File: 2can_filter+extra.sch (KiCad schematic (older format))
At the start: 25 parts, among them J5 54819-0572, J6 NOT_FITTED_SWD_Conn_01x04_Male, U10 74HC4050D, U11 TJA1040T, U12 TJA1040T, U8 74HC4050D, U9 STM32F105RBTx, Y2 Crystal KX-13 25MHz

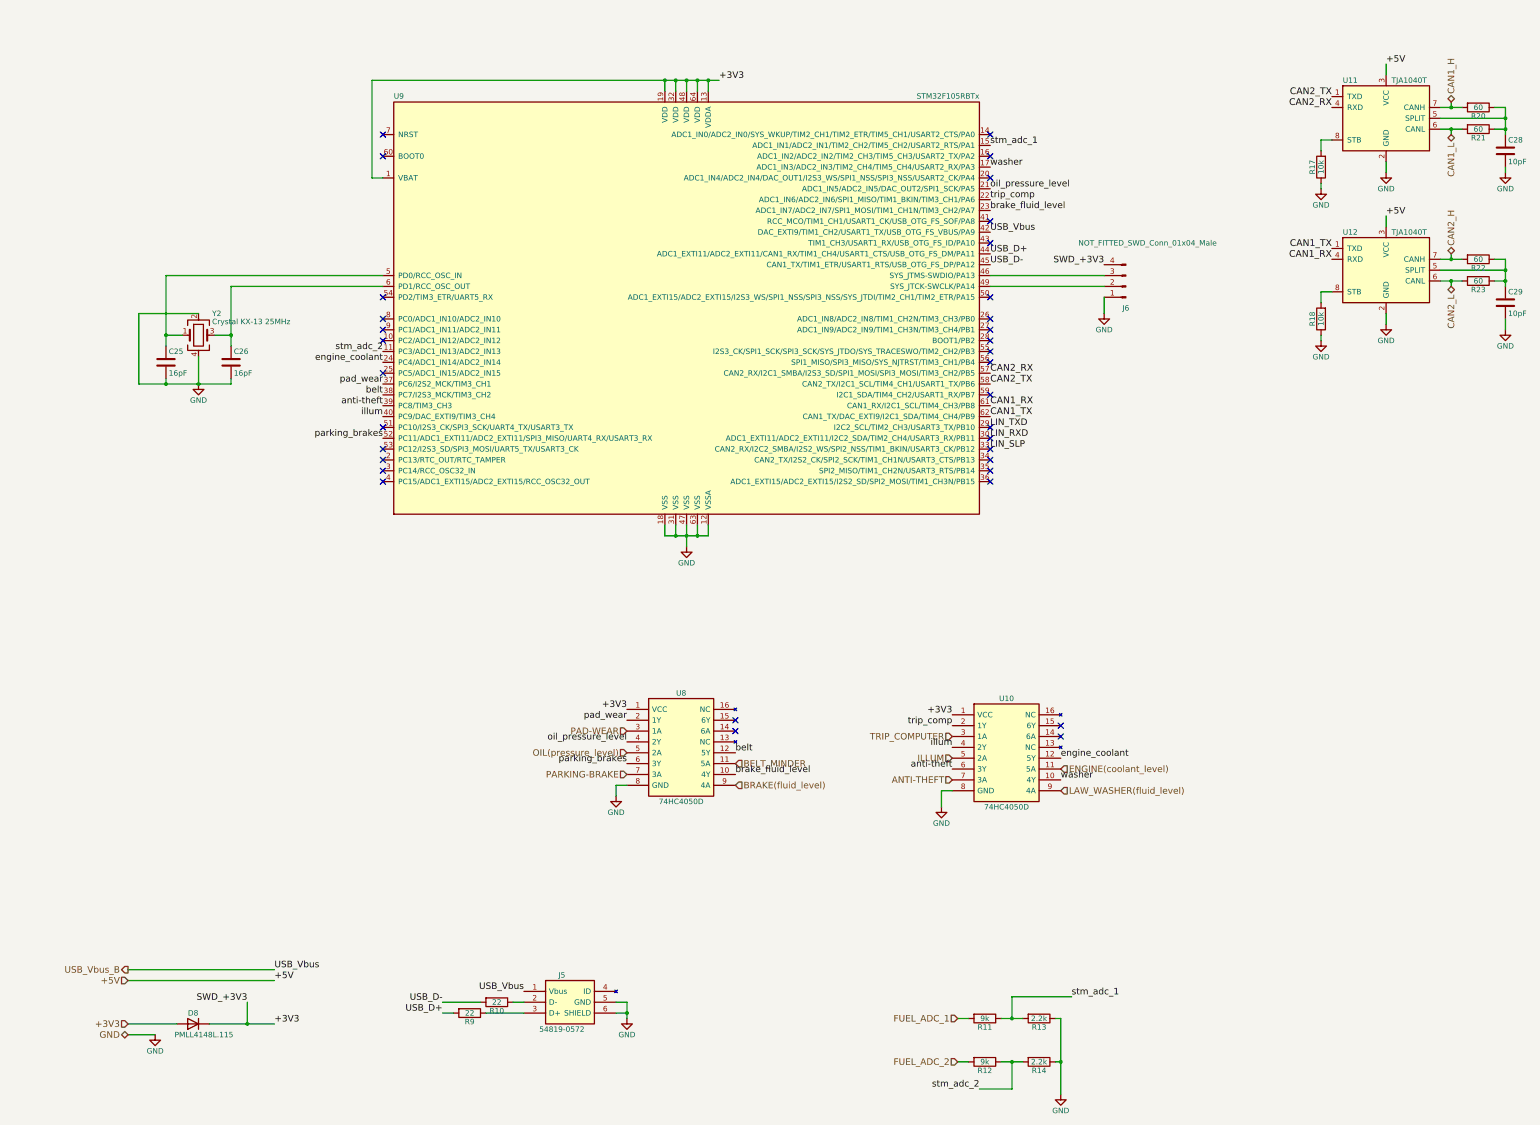
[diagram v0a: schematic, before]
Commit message: change connectivity of level-shifters(on sheme and pcb)
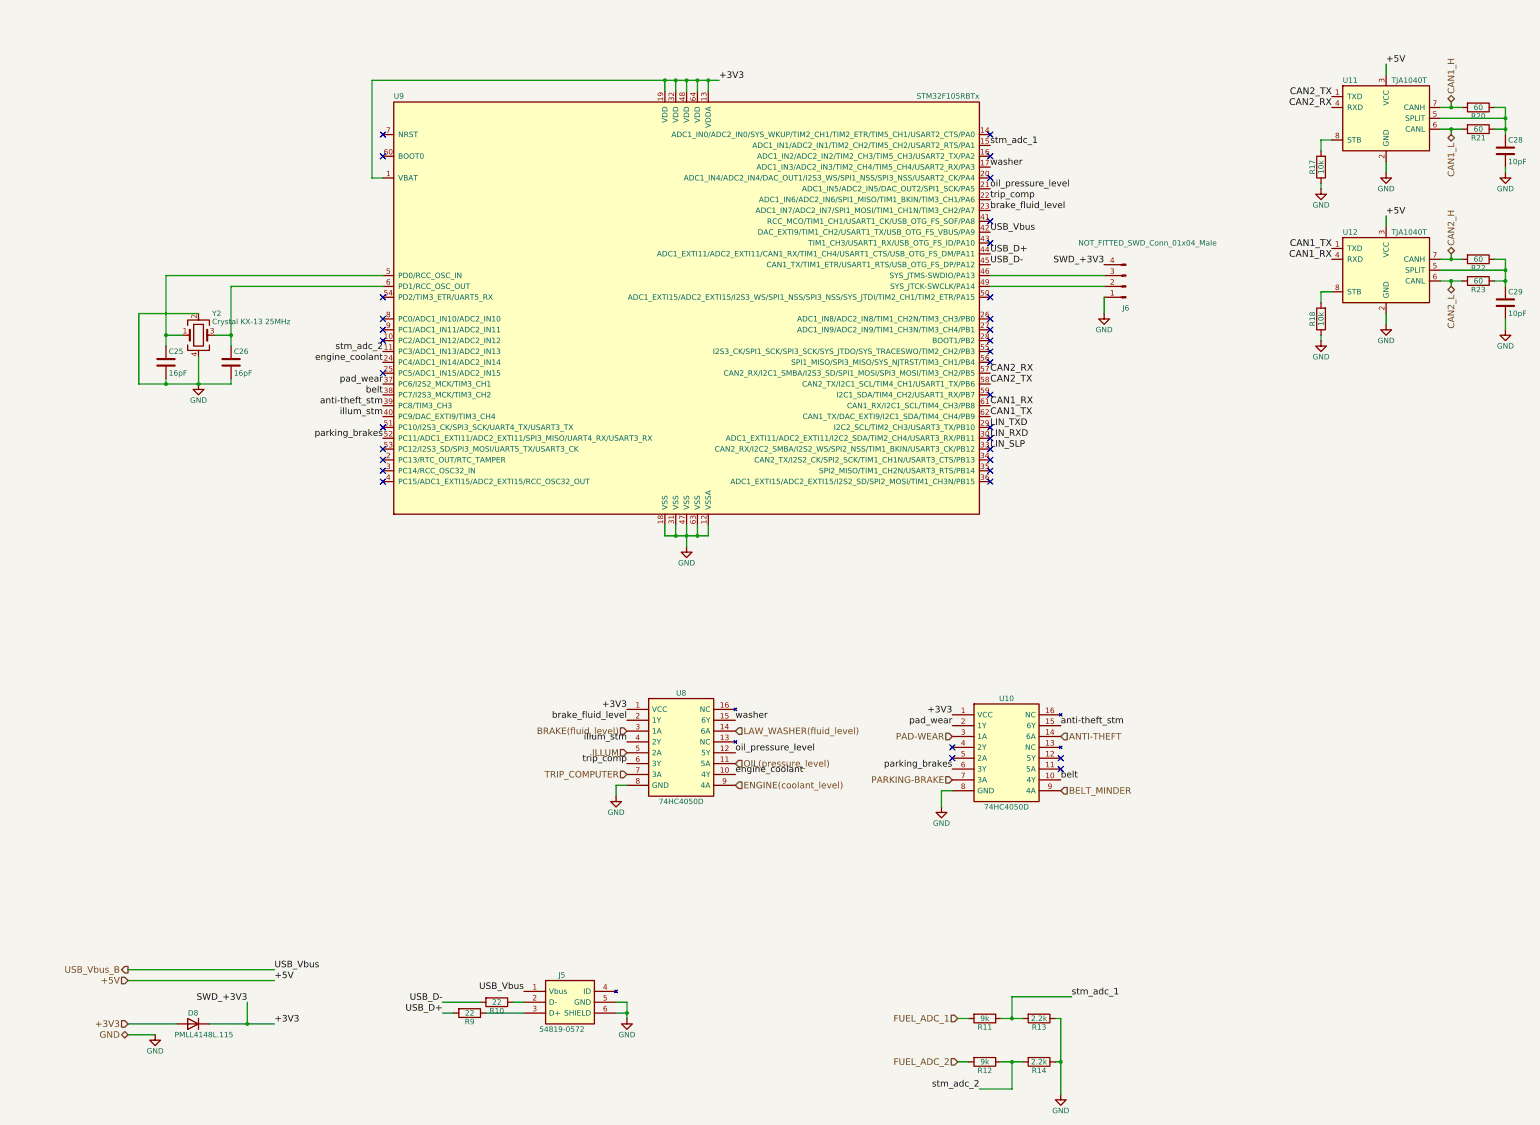
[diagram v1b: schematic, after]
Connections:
- net ANTI-THEFT: now also U10.14 (6A); no longer U10.7 (3A)
- net BELT_MINDER: now also U10.9 (4A); no longer U8.11 (5A)
- net BRAKE(fluid_level): now also U8.3 (1A); no longer U8.9 (4A)
- net ENGINE(coolant_level): now also U8.9 (4A); no longer U10.11 (5A)
- net ILLUM: now also U8.5 (2A); no longer U10.5 (2A)
- net LAW_WASHER(fluid_level): now also U8.14 (6A); no longer U10.9 (4A)
- net OIL(pressure_level): now also U8.11 (5A); no longer U8.5 (2A)
- net PAD-WEAR: now also U10.3 (1A); no longer U8.3 (1A)
- net PARKING-BRAKE: now also U10.7 (3A); no longer U8.7 (3A)
- net TRIP_COMPUTER: now also U8.7 (3A); no longer U10.3 (1A)
- net belt: now also U10.10 (4Y); no longer U8.12 (5Y)
- net brake_fluid_level: now also U8.2 (1Y); no longer U8.10 (4Y)
- net engine_coolant: now also U8.10 (4Y); no longer U10.12 (5Y)
- net oil_pressure_level: now also U8.12 (5Y); no longer U8.4 (2Y)
- net pad_wear: now also U10.2 (1Y); no longer U8.2 (1Y)
- net parking_brakes: now also U10.6 (3Y); no longer U8.6 (3Y)
- net trip_comp: now also U8.6 (3Y); no longer U10.2 (1Y)
- net washer: now also U8.15 (6Y); no longer U10.10 (4Y)
- net anti-theft_stm: now reaches U10.15 (6Y)
- net anti-theft_stm: now also U9.39 (PC8/TIM3_CH3)
- removed net anti-theft: U10.6 (3Y), U9.39 (PC8/TIM3_CH3)
- net illum: no longer names the net of U10.4 (2Y)
- net illum: no longer U9.40 (PC9/DAC_EXTI9/TIM3_CH4)
- new net illum_stm: U8.4 (2Y), U9.40 (PC9/DAC_EXTI9/TIM3_CH4)
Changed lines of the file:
@@
 $EndComp
 Wire Wire Line
-	13900 1500 14000 1500
-Wire Wire Line
-	14000 1500 14100 1500
+	13900 1500 14100 1500
 Wire Wire Line
 	14000 1450 14000 1500
@@
 $EndComp
 Wire Wire Line
-	4050 1250 6750 1250
-Wire Wire Line
-	6750 1250 6850 1250
-Wire Wire Line
-	6850 1250 6950 1250
-Wire Wire Line
-	6950 1250 7050 1250
-Wire Wire Line
-	7050 1250 7150 1250
-Wire Wire Line
-	7150 1250 7250 1250
+	4050 1250 7250 1250
 Wire Wire Line
 	7150 1250 7150 1350
@@
 	6750 5350 6750 5450
 Wire Wire Line
-	6750 5450 6850 5450
-Wire Wire Line
-	6850 5450 6950 5450
-Wire Wire Line
-	6950 5450 7050 5450
-Wire Wire Line
-	7050 5450 7150 5450
+	6750 5450 7150 5450
 Wire Wire Line
 	7150 5450 7150 5350
@@
 Connection ~ 7050 5450
 Wire Wire Line
-	6950 5350 6950 5450
-Wire Wire Line
-	6950 5450 6950 5550
+	6950 5350 6950 5550
 Connection ~ 6950 5450
 Wire Wire Line
@@
 +3V3
 Wire Wire Line
-	13900 1700 14000 1700
-Wire Wire Line
-	14000 1700 14100 1700
+	13900 1700 14100 1700
 Wire Wire Line
 	14000 1750 14000 1700
@@
 	13900 1600 14500 1600
 Wire Wire Line
-	14500 1500 14500 1600
-Wire Wire Line
-	14500 1600 14500 1700
-Wire Wire Line
-	14500 1700 14500 1750
+	14500 1500 14500 1750
 Wire Wire Line
 	14500 1700 14400 1700
@@
 	13900 3000 14500 3000
 Wire Wire Line
-	14500 2900 14500 3000
-Wire Wire Line
-	14500 3000 14500 3100
-Wire Wire Line
-	14500 3100 14500 3150
+	14500 2900 14500 3150
 Wire Wire Line
 	14500 3100 14400 3100
@@
 Connection ~ 14500 3000
 Wire Wire Line
-	13900 2900 14000 2900
-Wire Wire Line
-	14000 2900 14100 2900
+	13900 2900 14100 2900
 Wire Wire Line
 	14000 2850 14000 2900
 Connection ~ 14000 2900
 Wire Wire Line
-	13900 3100 14000 3100
-Wire Wire Line
-	14000 3100 14100 3100
+	13900 3100 14100 3100
 Wire Wire Line
 	14000 3150 14000 3100
@@
 SWD_+3V3
 Wire Wire Line
-	2550 9950 2900 9950
-Wire Wire Line
-	2900 9950 3150 9950
+	2550 9950 3150 9950
 Wire Wire Line
 	2900 9750 2900 9950
@@
 	2750 4050 2750 4000
 Wire Wire Line
-	2150 3050 2150 3600
-Wire Wire Line
-	2150 3600 2150 3700
+	2150 3050 2150 3700
 Wire Wire Line
 	2150 3600 2300 3600
@@
 	2600 3600 2750 3600
 Wire Wire Line
-	2750 3150 2750 3600
-Wire Wire Line
-	2750 3600 2750 3700
+	2750 3150 2750 3700
 Connection ~ 2150 3600
 Connection ~ 2750 3600
@@
 	6300 9750 6400 9750
 Wire Wire Line
-	6400 9750 6400 9850
-Wire Wire Line
-	6400 9850 6400 9900
+	6400 9750 6400 9900
+Text HLabel 6400 7650 0    60   Input ~ 0
+TRIP_COMPUTER
+Text HLabel 6400 7450 0    60   Input ~ 0
+ILLUM
+Text HLabel 10400 7300 2    60   Input ~ 0
+ANTI-THEFT
 Text HLabel 9400 7300 0    60   Input ~ 0
-TRIP_COMPUTER
-Text HLabel 9400 7500 0    60   Input ~ 0
-ILLUM
+PAD-WEAR
+Text HLabel 7400 7550 2    60   Input ~ 0
+OIL(pressure_level)
 Text HLabel 9400 7700 0    60   Input ~ 0
-ANTI-THEFT
-Text HLabel 6400 7250 0    60   Input ~ 0
-PAD-WEAR
-Text HLabel 6400 7450 0    60   Input ~ 0
-OIL(pressure_level)
-Text HLabel 6400 7650 0    60   Input ~ 0
 PARKING-BRAKE
 Text HLabel 9450 9900 0    60   Input ~ 0
@@
 Text HLabel 9450 10300 0    60   Input ~ 0
 FUEL_ADC_2
-Text HLabel 10400 7600 2    60   Input ~ 0
+Text HLabel 7400 7750 2    60   Input ~ 0
 ENGINE(coolant_level)
+Text HLabel 7400 7250 2    60   Input ~ 0
+LAW_WASHER(fluid_level)
+Text HLabel 6400 7250 0    60   Input ~ 0
+BRAKE(fluid_level)
 Text HLabel 10400 7800 2    60   Input ~ 0
-LAW_WASHER(fluid_level)
-Text HLabel 7400 7750 2    60   Input ~ 0
-BRAKE(fluid_level)
-Text HLabel 7400 7550 2    60   Input ~ 0
 BELT_MINDER
 Text Label 9400 7100 2    60   ~ 0
@@
 $EndComp
 Wire Wire Line
-	9850 9900 9950 9900
-Wire Wire Line
-	9950 9900 10050 9900
+	9850 9900 10050 9900
 Wire Wire Line
 	9550 9900 9450 9900
@@
 $EndComp
 Wire Wire Line
-	9850 10300 9950 10300
-Wire Wire Line
-	9950 10300 10050 10300
+	9850 10300 10050 10300
 Wire Wire Line
 	9550 10300 9450 10300
@@
 $EndComp
 Wire Wire Line
-	10400 9900 10400 10300
-Wire Wire Line
-	10400 10300 10400 10600
+	10400 9900 10400 10600
 Connection ~ 10400 10300
 Text Label 10500 9700 0    60   ~ 0
@@
 Wire Wire Line
 	2750 3150 4150 3150
-NoConn ~ 10400 7300
-NoConn ~ 10400 7200
-NoConn ~ 7400 7250
-NoConn ~ 7400 7150
-Text Label 9400 7200 2    60   ~ 0
+Text Label 6400 7550 2    60   ~ 0
 trip_comp
-Text Label 9400 7400 2    60   ~ 0
-illum
-Text Label 9400 7600 2    60   ~ 0
-anti-theft
+Text Label 6400 7350 2    60   ~ 0
+illum_stm
+Text Label 10400 7200 0    60   ~ 0
+anti-theft_stm
 $Comp
 L GND #PWR043
@@
 Wire Wire Line
 	6300 7750 6400 7750
+Text Label 7400 7150 0    60   ~ 0
+washer
+Text Label 7400 7650 0    60   ~ 0
+engine_coolant
 Text Label 10400 7700 0    60   ~ 0
-washer
-Text Label 10400 7500 0    60   ~ 0
-engine_coolant
+belt
+Text Label 6400 7150 2    60   ~ 0
+brake_fluid_level
+Text Label 9400 7600 2    60   ~ 0
+parking_brakes
+Text Label 9400 7200 2    60   ~ 0
+pad_wear
 Text Label 7400 7450 0    60   ~ 0
-belt
-Text Label 7400 7650 0    60   ~ 0
-brake_fluid_level
-Text Label 6400 7550 2    60   ~ 0
-parking_brakes
-Text Label 6400 7150 2    60   ~ 0
-pad_wear
-Text Label 6400 7350 2    60   ~ 0
 oil_pressure_level
 Text Label 4150 4550 2    60   ~ 0
@@
 trip_comp
 Text Label 4150 4250 2    60   ~ 0
-anti-theft
-Text Label 4150 4350 2    60   ~ 0
-illum
+anti-theft_stm
 NoConn ~ 4150 4650
 NoConn ~ 4150 4750
@@
 	2450 4050 2450 3800
 Wire Wire Line
-	1900 4050 2150 4050
-Wire Wire Line
-	2150 4050 2450 4050
-Wire Wire Line
-	2450 4050 2750 4050
+	1900 4050 2750 4050
 Connection ~ 2450 4050
 Wire Wire Line
@@
 Text Label 4150 3750 2    60   ~ 0
 stm_adc_2
+NoConn ~ 9400 7400
+NoConn ~ 9400 7500
+NoConn ~ 10400 7500
+NoConn ~ 10400 7600
+Text Label 4150 4350 2    60   ~ 0
+illum_stm
 $EndSCHEMATC

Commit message: redone shematic of power supply, fix usb_vbus and swd diods connections, change mcu capacitors connections
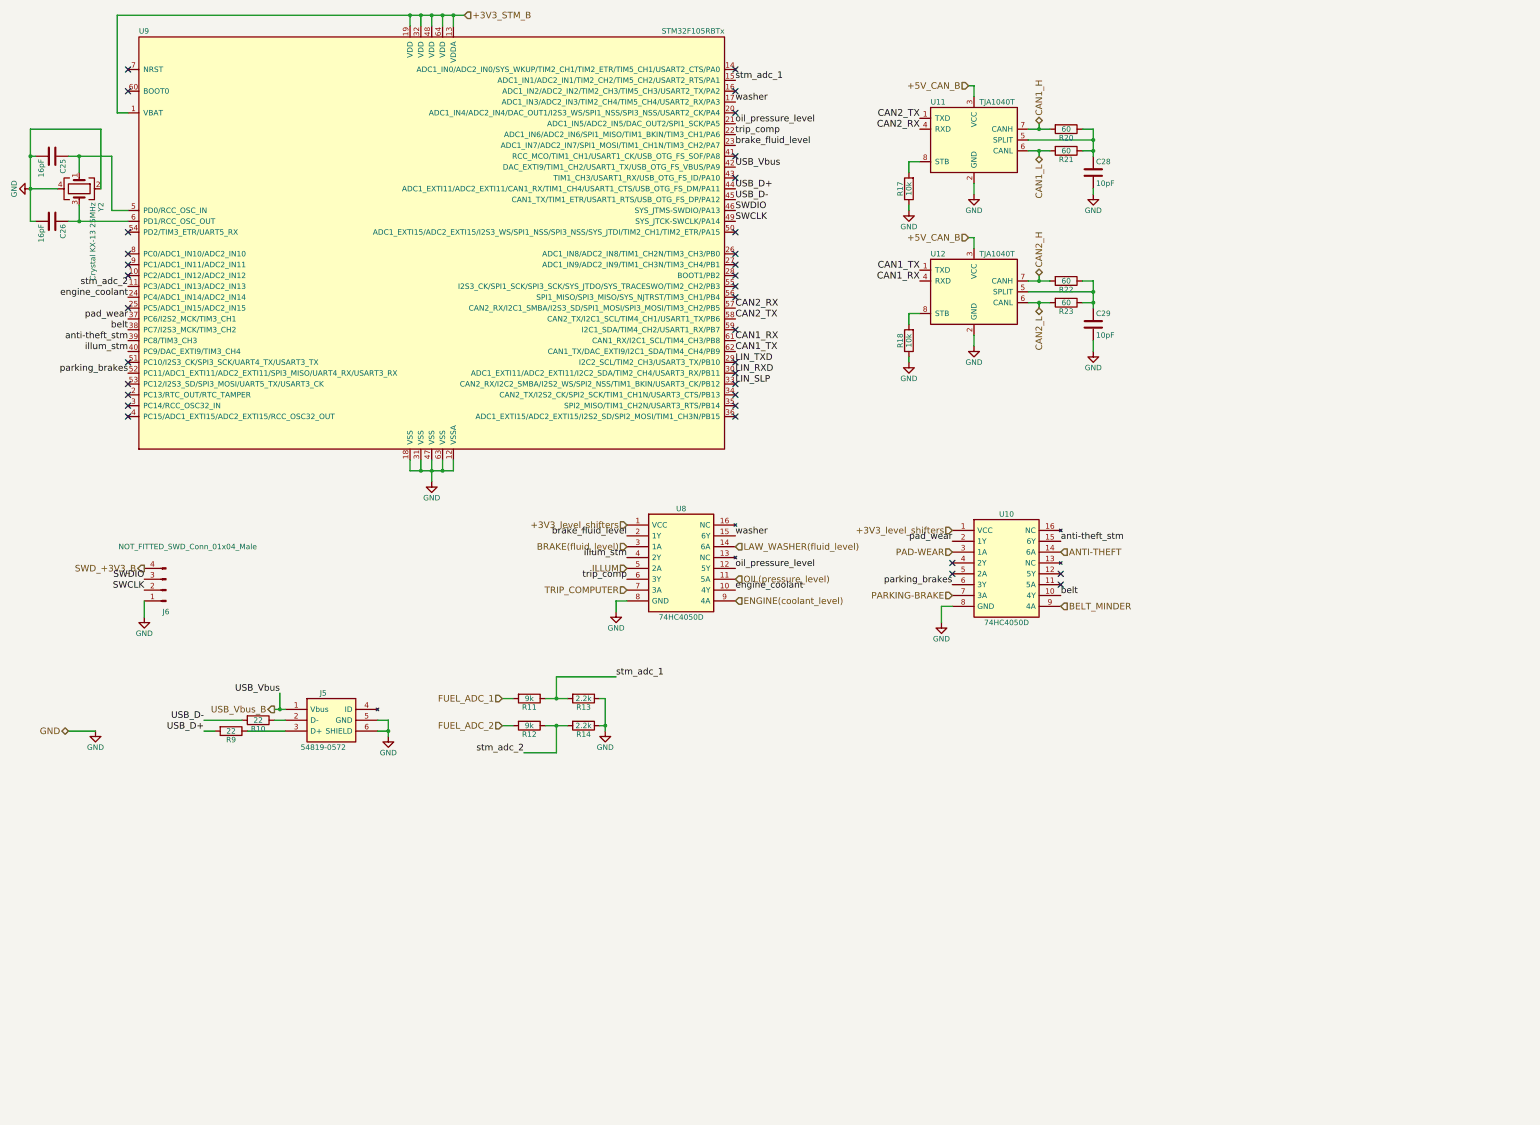
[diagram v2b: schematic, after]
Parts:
- removed D8: PMLL4148L.115, Diodes_SMD:D_SC-80, symbol D
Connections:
- net SWDIO: now reaches J6.3 (Pin_3), U9.46 (SYS_JTMS-SWDIO/PA13)
- net SWCLK: now reaches J6.2 (Pin_2), U9.49 (SYS_JTCK-SWCLK/PA14)
- net +3V3 renamed +3V3_STM_B
- net +3V3_STM_B: no longer J6.4 (Pin_4), U10.1 (VCC), U8.1 (VCC)
- net +5V renamed +5V_CAN_B
- new net +3V3_level_shifters: U10.1 (VCC), U8.1 (VCC)
- new net SWD_+3V3_B: J6.4 (Pin_4)
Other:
- moved on the sheet: C25, C26, C28, C29, J5, J6, R10, R11, R12, R13, R14, R17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
